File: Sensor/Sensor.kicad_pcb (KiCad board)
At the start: 2 copper layers, 17 parts, among them J1 Signal, J2 Power, U1 LBR-127HLD, U2 LBR-127HLD, U3 LBR-127HLD, U4 LBR-127HLD, U5 LBR-127HLD

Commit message: センサー関係忘れてた
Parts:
- added D1: LED, LED_SMD:LED_0603_1608Metric, F.Cu at (32.2, 56.6)
- added D2: LED, LED_SMD:LED_0603_1608Metric, F.Cu at (32.2, 59.2)
- added D3: LED, LED_SMD:LED_0603_1608Metric, F.Cu at (32.2, 61.8)
- added D4: LED, LED_SMD:LED_0603_1608Metric, F.Cu at (32.2, 64.3)
- added D5: LED, LED_SMD:LED_0603_1608Metric, F.Cu at (32.2, 66.9)
- added U6: 74HC244, Package_SO:SSOP-20_4.4x6.5mm_P0.65mm, F.Cu at (39.0, 59.3)
- R1: value 200 -> 220; footprint Resistor_THT:R_Axial_DIN0207_L6.3mm_D2.5mm_P10.16mm_Horizontal -> Resistor_SMD:R_0603_1608Metric
- R10, R2, R3, R4, R5, R6, R7, R8, R9: footprint Resistor_THT:R_Axial_DIN0207_L6.3mm_D2.5mm_P10.16mm_Horizontal -> Resistor_SMD:R_0603_1608Metric
- U1, U2, U3, U4, U5: moved to B.Cu
- moved R2 98.4 mm to (22.7, 22.0), turned to 0 degrees
- moved R3 85.2 mm to (22.7, 26.1), turned to 0 degrees
- moved J2 77.8 mm to (47.0, 33.0), turned to 0 degrees
- moved R1 76.2 mm to (48.9, 35.6), turned to -90 degrees
- moved R5 71.5 mm to (22.7, 34.2), turned to 0 degrees
- moved U1 59.9 mm to (53.3, 42.4)
- moved R7 58.6 mm to (22.7, 42.3), turned to 0 degrees
- moved R4 54.9 mm to (57.8, 35.6), turned to -90 degrees
- moved J1 52.6 mm to (47.0, 18.3), turned to 0 degrees
- moved R9 46.9 mm to (22.7, 50.4), turned to 0 degrees
- moved U2 38.4 mm to (62.2, 42.4)
- moved R6 33.9 mm to (66.7, 35.6), turned to -90 degrees
- moved U5 26.9 mm to (88.7, 42.4)
- moved U3 17.2 mm to (71.1, 42.4)
- moved R8 14.8 mm to (75.6, 35.6), turned to -90 degrees
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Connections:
- U1 pad 3: O1 -> GND
- U1 pad 4: GND -> O1
- U2 pad 3: O2 -> GND
- U2 pad 4: GND -> O2
- U3 pad 3: O3 -> GND
- U3 pad 4: GND -> O3
- U4 pad 3: O4 -> GND
- U4 pad 4: GND -> O4
- U5 pad 3: O5 -> GND
- U5 pad 4: GND -> O5

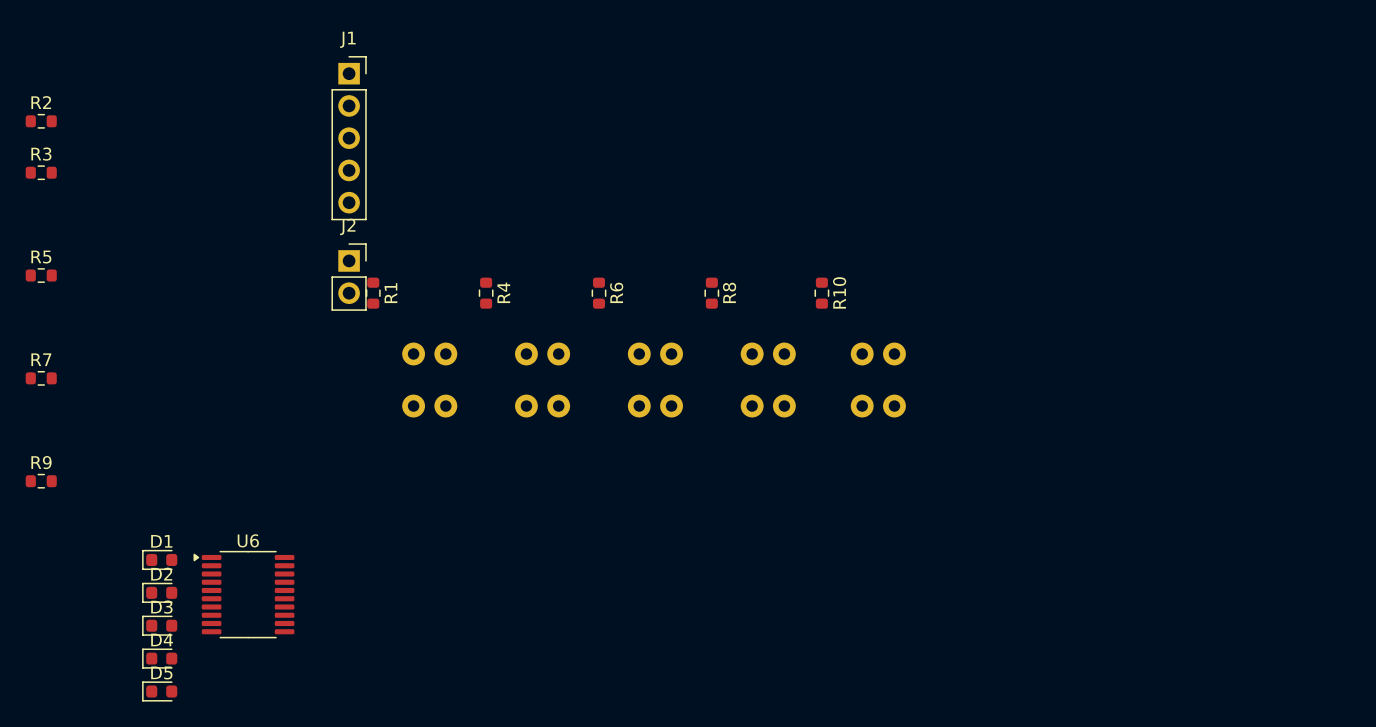
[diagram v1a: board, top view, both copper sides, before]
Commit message: 出力を追加
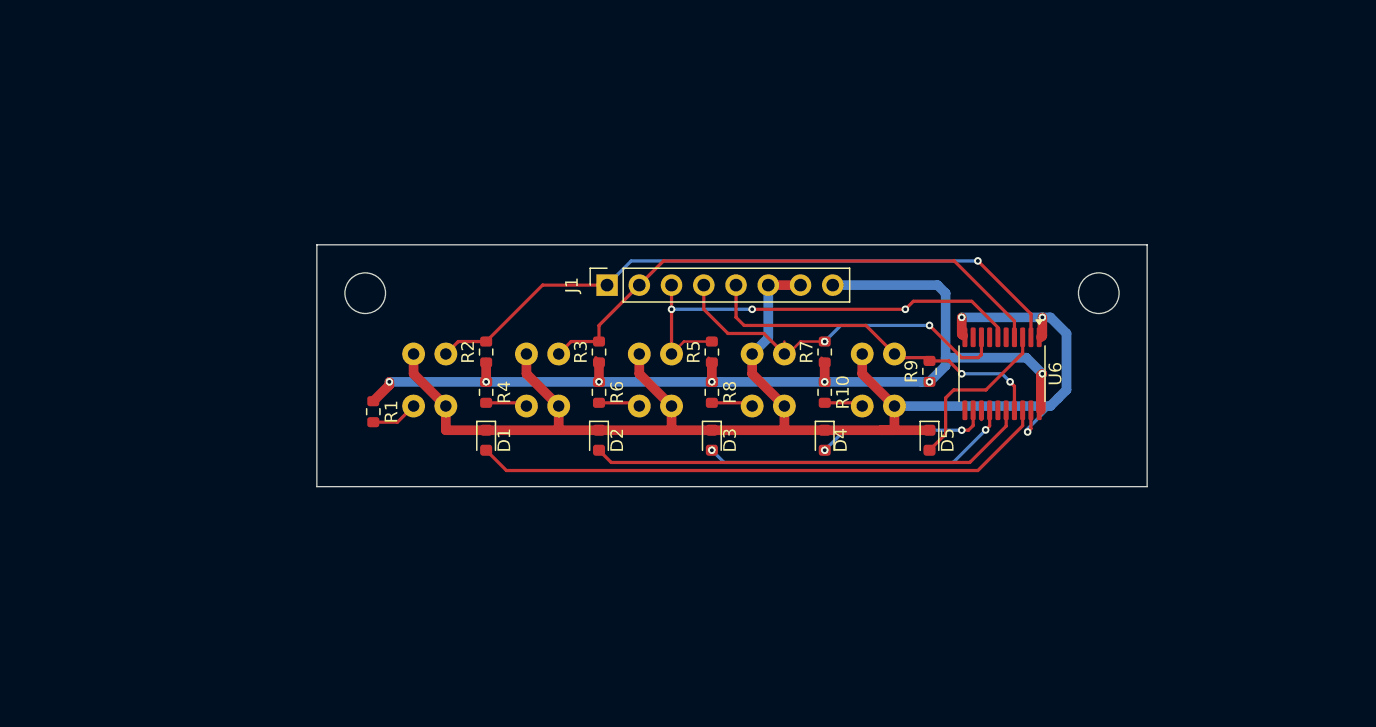
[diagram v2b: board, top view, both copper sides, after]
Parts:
- removed J2: Power, Connector_PinSocket_2.54mm:PinSocket_1x02_P2.54mm_Vertical
- added REF**: MountingHole_3.2mm_M3, MountingHole:MountingHole_3.2mm_M3, F.Cu at (106.0, 35.6)
- added REF**: MountingHole_3.2mm_M3, MountingHole:MountingHole_3.2mm_M3, F.Cu at (48.3, 35.6)
- J1: value Signal -> Conn_01x08_Socket; footprint Connector_PinSocket_2.54mm:PinSocket_1x05_P2.54mm_Vertical -> Connector_PinSocket_2.54mm:PinSocket_1x08_P2.54mm_Vertical
- moved R9 70.5 mm to (92.7, 41.7), turned to 90 degrees
- moved D5 63.6 mm to (92.7, 47.1), turned to -90 degrees
- moved U6 61.9 mm to (98.4, 41.9), turned to -90 degrees
- moved R7 61.7 mm to (84.5, 40.2), turned to 90 degrees
- moved D4 55.0 mm to (84.5, 47.1), turned to -90 degrees
- moved R5 53.2 mm to (75.6, 40.2), turned to 90 degrees
- moved R3 46.1 mm to (66.7, 40.2), turned to 90 degrees
- moved D3 45.7 mm to (75.6, 47.1), turned to -90 degrees
- moved R2 39.5 mm to (57.8, 40.2), turned to 90 degrees
- moved D2 36.5 mm to (66.7, 47.1), turned to -90 degrees
- moved D1 27.2 mm to (57.8, 47.1), turned to -90 degrees
- moved J1 26.3 mm to (67.3, 34.9), turned to 90 degrees
- moved R1 9.34 mm to (48.9, 44.9)
- moved R10 7.81 mm to (84.5, 43.4)
- moved R4 7.81 mm to (57.8, 43.4)
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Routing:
- net GND: track 0.00 -> 118.9 mm, vias 0 -> 3
- net VCC: track 0.00 -> 80.1 mm, vias 0 -> 7
- net O1: track 0.00 -> 53.1 mm, vias 0 -> 1
- net Net-(D1-A): track 0.00 -> 45.6 mm
- net O2: track 0.00 -> 43.3 mm
- net O3: track 0.00 -> 37.0 mm, vias 0 -> 3
- net Net-(D2-A): track 0.00 -> 34.9 mm
- net O4: track 0.00 -> 30.1 mm, vias 0 -> 2
- net O5: track 0.00 -> 28.6 mm, vias 0 -> 2
- net Net-(D3-A): track 0.00 -> 24.7 mm, vias 0 -> 2
- net Net-(D4-A): track 0.00 -> 13.7 mm, vias 0 -> 2
- net Net-(D5-A): track 0.00 -> 13.4 mm
- net Net-(U1-Anode): track 0.00 -> 3.70 mm
- net Net-(U2-Anode): track 0.00 -> 3.28 mm
- net Net-(U4-Anode): track 0.00 -> 3.28 mm
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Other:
- board outline added: 65.4 x 19 mm
